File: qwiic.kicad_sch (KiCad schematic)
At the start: 3 parts, among them J7 JST_SH_1x4_BM04B-SRSS-TB-LF-SN

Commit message: [#93514] Propagate title and date across all of the sheets
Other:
- title: (none) -> Datacenter Secure Control Module Breakout Board
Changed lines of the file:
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@@
 	(generator_version "9.0")
 	(paper "A3")
+	(title_block
+		(title "Datacenter Secure Control Module Breakout Board")
+		(date "2021-12-16")
+		(rev "2.0.0")
+	)
 	(text "QWIIC"
 		(exclude_from_sim no)

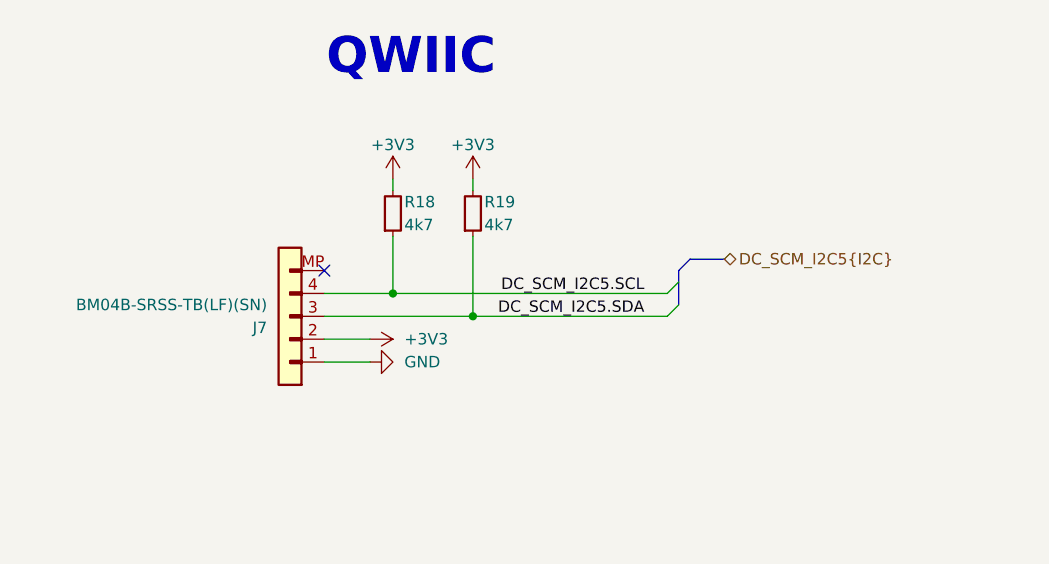
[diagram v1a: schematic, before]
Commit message: [#93514] Add TVS to QWIIC
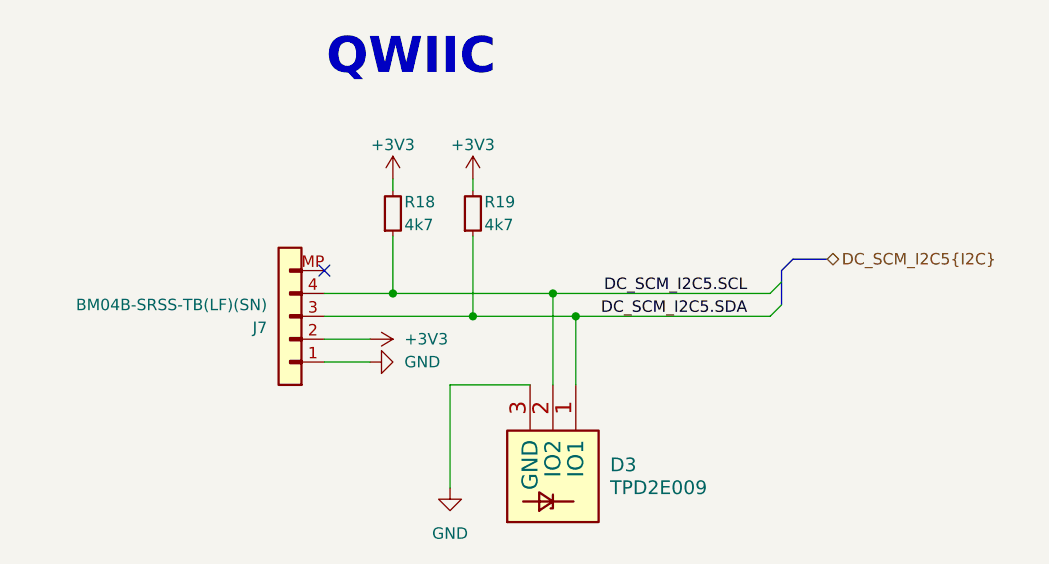
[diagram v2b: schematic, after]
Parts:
- added D3: TPD2E009, bmc-breakout-board-footprints:SOT-3, symbol bmc-breakout-board:TPD2E009
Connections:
- net DC_SCM_I2C5.SCL: now also D3.2 (IO2)
- net DC_SCM_I2C5.SDA: now also D3.1 (IO1)
- net GND: now also D3.3 (GND)
